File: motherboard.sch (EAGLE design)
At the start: 34 parts

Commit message: more routing
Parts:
- added CONN: BOURNS_2PIN, CUSTOM:BOURNS_2PIN
- added R11, R12: 100, resistor:R-US_R0603
- added U$2: BI_LED, CUSTOM:BI_LED
- added U$3: 4PIN_HEADER, CUSTOM:4PIN_HEADER
- KEY: value PTS645 -> PTS810
- R9: value 33k -> 5k
- renumbered U$1 to WIPER
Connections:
- removed net GP14: ESP12.GPIO14
- removed net GP16: ESP12.GPIO16
- removed net N$3: D1.AN, MICRO-USB.V+
- new net N$11: R11.1, U$2.2
- new net N$12: R12.1, U$2.3
- new net N$8: ESP12.GPIO14, R12.2
- new net N$9: ESP12.GPIO16, R11.2
- new net USB+: D1.AN, MICRO-USB.V+, U$3.1
- net D+: now also U$3.3
- net D-: now also U$3.2
- net GND: now also CONN.P2, U$2.1, U$2.4, U$3.4, WIPER.P2; no longer WIPER.P3
- net VCC: now also CONN.P1, WIPER.P3; no longer WIPER.P2
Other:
- moved on the sheet: D1, KEY

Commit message: final routing before splitting up boards
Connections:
- net GND: now also KEY.4; no longer KEY.3
- net RST: now also KEY.2; no longer KEY.1
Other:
- moved on the sheet: KEY
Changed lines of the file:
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@@
 <instance part="R7" gate="G$1" x="35.56" y="149.86"/>
 <instance part="R6" gate="G$1" x="35.56" y="142.24"/>
-<instance part="KEY" gate="G$1" x="170.18" y="187.96"/>
+<instance part="KEY" gate="G$1" x="142.24" y="187.96"/>
 <instance part="D1" gate="G$1" x="12.7" y="144.78" rot="R90"/>
 <instance part="P+3" gate="VCC" x="12.7" y="157.48"/>
@@
 <net name="GND" class="0">
 <segment>
-<wire x1="162.56" y1="182.88" x2="152.4" y2="182.88" width="0.1524" layer="91"/>
 <pinref part="GND5" gate="1" pin="GND"/>
 <wire x1="152.4" y1="180.34" x2="152.4" y2="182.88" width="0.1524" layer="91"/>
-<pinref part="KEY" gate="G$1" pin="3"/>
+<pinref part="KEY" gate="G$1" pin="4"/>
+<wire x1="152.4" y1="182.88" x2="149.86" y2="182.88" width="0.1524" layer="91"/>
 </segment>
 <segment>
@@
 <net name="RST" class="0">
 <segment>
-<label x="152.4" y="193.04" size="1.778" layer="95"/>
-<pinref part="KEY" gate="G$1" pin="1"/>
-<wire x1="162.56" y1="193.04" x2="152.4" y2="193.04" width="0.1524" layer="91"/>
-</segment>
-<segment>
 <pinref part="R2" gate="G$1" pin="2"/>
 <wire x1="203.2" y1="185.42" x2="215.9" y2="185.42" width="0.1524" layer="91"/>
@@
 <label x="35.56" y="63.5" size="1.778" layer="95"/>
 </segment>
+<segment>
+<pinref part="KEY" gate="G$1" pin="2"/>
+<wire x1="149.86" y1="193.04" x2="157.48" y2="193.04" width="0.1524" layer="91"/>
+<label x="152.4" y="193.04" size="1.778" layer="95"/>
+</segment>
 </net>

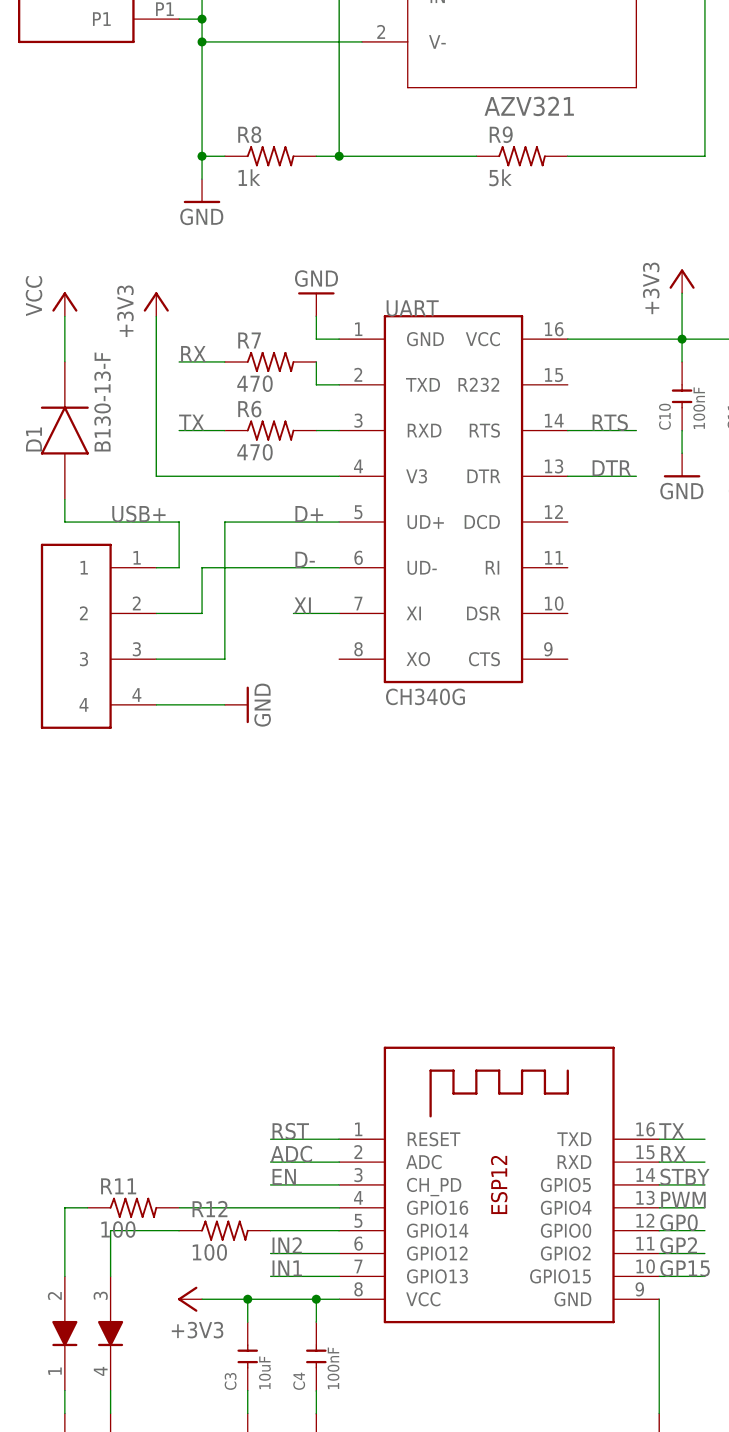
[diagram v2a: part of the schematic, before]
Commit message: Added BOM, updated resistor values
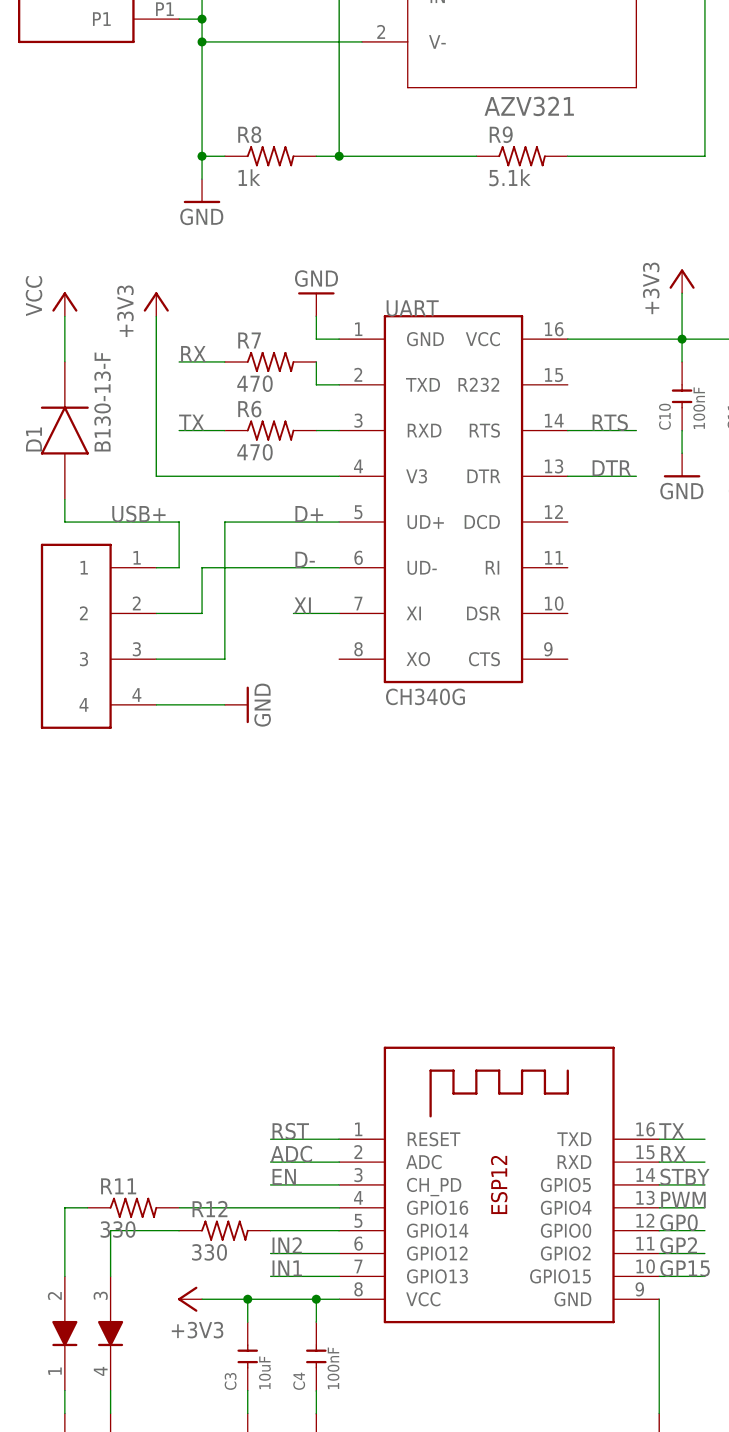
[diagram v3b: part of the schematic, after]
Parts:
- R11, R12: value 100 -> 330
- R9: value 5k -> 5.1k
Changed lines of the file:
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@@
 <part name="D1" library="CUSTOM" deviceset="B130-13-F" device=""/>
 <part name="P+3" library="supply1" deviceset="VCC" device=""/>
-<part name="R9" library="resistor" deviceset="R-US_" device="R0603" value="5k"/>
+<part name="R9" library="resistor" deviceset="R-US_" device="R0603" value="5.1k"/>
 <part name="R8" library="resistor" deviceset="R-US_" device="R0603" value="1k"/>
 <part name="GND15" library="supply1" deviceset="GND" device=""/>
@@
 <part name="P+2" library="supply1" deviceset="VCC" device=""/>
 <part name="U$2" library="CUSTOM" deviceset="BI_LED" device=""/>
-<part name="R11" library="resistor" deviceset="R-US_" device="R0603" value="100"/>
-<part name="R12" library="resistor" deviceset="R-US_" device="R0603" value="100"/>
+<part name="R11" library="resistor" deviceset="R-US_" device="R0603" value="330"/>
+<part name="R12" library="resistor" deviceset="R-US_" device="R0603" value="330"/>
 <part name="U$3" library="CUSTOM" deviceset="4PIN_HEADER" device=""/>
 <part name="GND7" library="supply1" deviceset="GND" device=""/>
